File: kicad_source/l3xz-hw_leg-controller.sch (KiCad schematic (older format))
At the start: 37 parts, among them CN1 ARDUINO_NANO_33, CN2 SM04B-SRSS-TB, CN3 SM04B-SRSS-TB, CN6 691322310002, CN7 CONN_02X03, CN8 WAGO 733-362, U3 24LC64

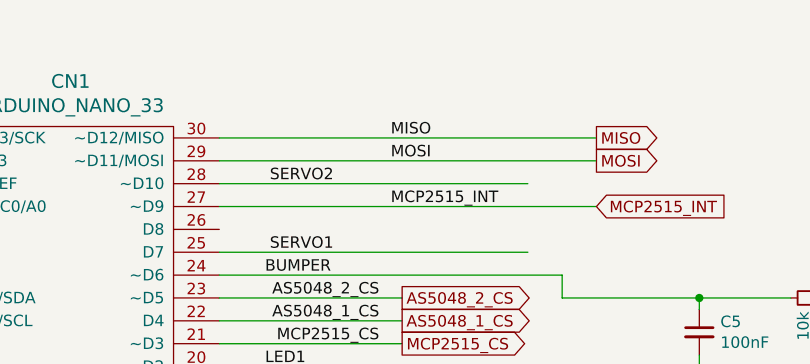
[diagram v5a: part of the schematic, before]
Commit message: fixed crystal issues, corrected CAN driver footprint, added pullup on MISO
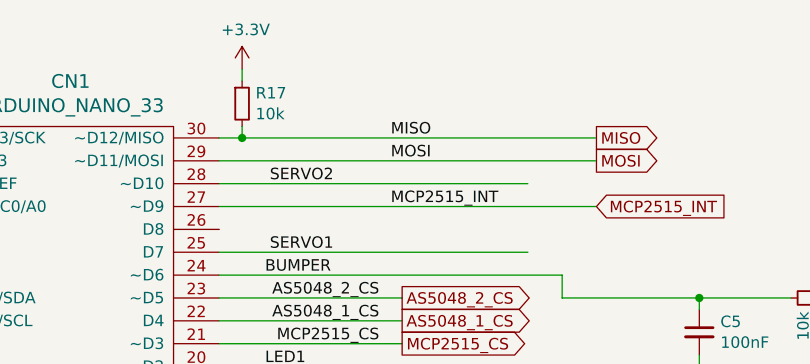
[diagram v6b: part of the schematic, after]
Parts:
- added R17: 10k, resistors:R_0603, symbol devices:R_0603
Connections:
- wire segments 112 -> 115
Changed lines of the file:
@@
 MISO
 Wire Wire Line
-	6300 1350 4650 1350
+	6300 1350 4750 1350
 Wire Wire Line
 	3350 1350 1700 1350
@@
 Text Notes 6400 5050 0    50   ~ 0
 30V 500mA
+$Comp
+L power-supply:+3.3V #PWR?
+U 1 1 629F7BED
+P 4750 1050
+AR Path="/5ED92F9C/629F7BED" Ref="#PWR?"  Part="1"
+AR Path="/629F7BED" Ref="#PWR054"  Part="1"
+F 0 "#PWR054" H 4750 900 50  0001 C CNN
+F 1 "+3.3V" H 4765 1223 50  0000 C CNN
+F 2 "" H 4750 1050 50  0000 C CNN
+F 3 "" H 4750 1050 50  0000 C CNN
+	1    4750 1050
+	1    0    0    -1
+$EndComp
+$Comp
+L devices:R_0603 R?
+U 1 1 629F7C9D
+P 4750 1200
+AR Path="/5ED92F9C/629F7C9D" Ref="R?"  Part="1"
+AR Path="/629F7C9D" Ref="R17"  Part="1"
+F 0 "R17" H 4809 1246 50  0000 L CNN
+F 1 "10k" H 4809 1155 50  0000 L CNN
+F 2 "resistors:R_0603" H 4750 1050 50  0001 C CNN
+F 3 "" H 4750 1200 50  0000 C CNN
+	1    4750 1200
+	1    0    0    -1
+$EndComp
+Wire Wire Line
+	4750 1100 4750 1050
+Wire Wire Line
+	4750 1300 4750 1350
+Connection ~ 4750 1350
+Wire Wire Line
+	4750 1350 4650 1350
 $EndSCHEMATC
